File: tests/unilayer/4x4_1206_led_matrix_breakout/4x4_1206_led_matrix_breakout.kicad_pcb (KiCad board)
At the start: 2 copper layers, 22 x 26 mm, 22 parts, among them J1 Conn_01x04_Pin, J2 Conn_01x04_Pin

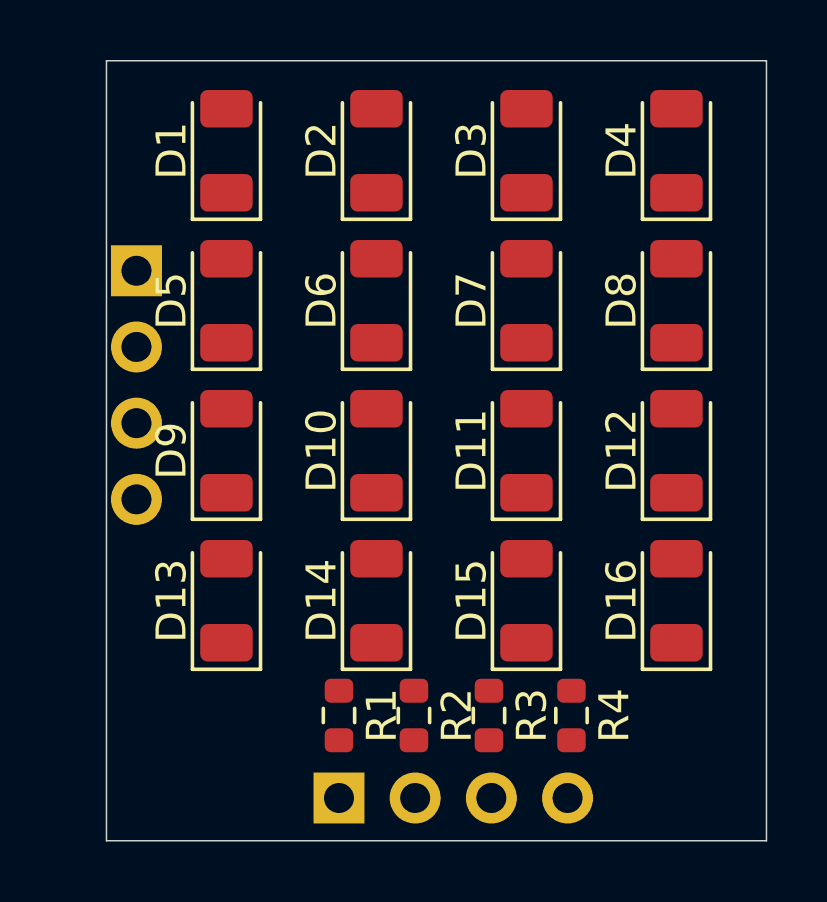
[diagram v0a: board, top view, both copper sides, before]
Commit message: chore: Add screenshot of autorouted 4x4_1206_matrix_breakout to gallery, with some small changes
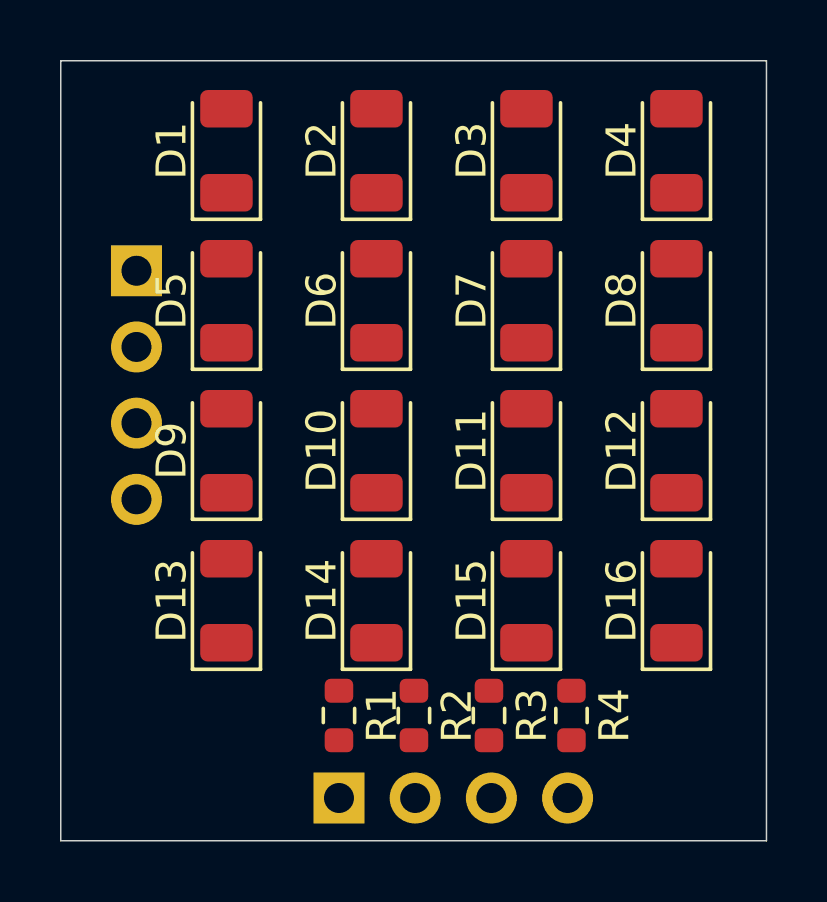
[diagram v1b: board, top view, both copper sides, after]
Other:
- board size 22 x 26 mm -> 23.5 x 26 mm
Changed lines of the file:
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@@
 			(at 0 1.83 90)
 			(layer "F.Fab")
+			(hide yes)
 			(effects
 				(font
@@
 			(at 0 1.83 90)
 			(layer "F.Fab")
+			(hide yes)
 			(effects
 				(font
@@
 			(at 0 1.83 90)
 			(layer "F.Fab")
+			(hide yes)
 			(effects
 				(font
@@
 			(at 0 1.83 90)
 			(layer "F.Fab")
+			(hide yes)
 			(effects
 				(font
@@
 			(at 0 1.83 90)
 			(layer "F.Fab")
+			(hide yes)
 			(effects
 				(font
@@
 			(at 0 1.83 90)
 			(layer "F.Fab")
+			(hide yes)
 			(effects
 				(font
@@
 			(at 0 1.43 90)
 			(layer "F.Fab")
+			(hide yes)
 			(effects
 				(font
@@
 			(at 0 1.43 90)
 			(layer "F.Fab")
+			(hide yes)
 			(effects
 				(font
@@
 			(at 0 1.83 90)
 			(layer "F.Fab")
+			(hide yes)
 			(effects
 				(font
@@
 			(at 0 1.83 90)
 			(layer "F.Fab")
+			(hide yes)
 			(effects
 				(font
@@
 			(at 0 1.83 90)
 			(layer "F.Fab")
+			(hide yes)
 			(effects
 				(font
@@
 			(at 0 1.43 90)
 			(layer "F.Fab")
+			(hide yes)
 			(effects
 				(font
@@
 			(at 0 1.43 90)
 			(layer "F.Fab")
+			(hide yes)
 			(effects
 				(font
@@
 			(at 0 1.83 90)
 			(layer "F.Fab")
+			(hide yes)
 			(effects
 				(font
@@
 			(at 0 1.83 90)
 			(layer "F.Fab")
+			(hide yes)
 			(effects
 				(font
@@
 			(at 0 1.83 90)
 			(layer "F.Fab")
+			(hide yes)
 			(effects
 				(font
@@
 			(at 0 1.83 90)
 			(layer "F.Fab")
+			(hide yes)
 			(effects
 				(font
@@
 			(at 0 1.83 90)
 			(layer "F.Fab")
+			(hide yes)
 			(effects
 				(font
@@
 			(at 0 1.83 90)
 			(layer "F.Fab")
+			(hide yes)
 			(effects
 				(font
@@
 			(at 0 1.83 90)
 			(layer "F.Fab")
+			(hide yes)
 			(effects
 				(font
@@
 			(at 4.385 -9.89 0)
 			(layer "B.Fab")
+			(hide yes)
 			(effects
 				(font
@@
 			(at 4.385 -9.89 90)
 			(layer "B.Fab")
+			(hide yes)
 			(effects
 				(font
@@
 	)
 	(gr_rect
-		(start 136 72)
+		(start 134.476 72)
 		(end 158 98)
 		(stroke
